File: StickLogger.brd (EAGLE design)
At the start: 61 x 61 mm, 52 parts, among them IC1 4050D, U1 ATMEGA328P-MU, U4 DS1307, X1 MICROSD, Y1 16MHZ, Y2 32.768kHz

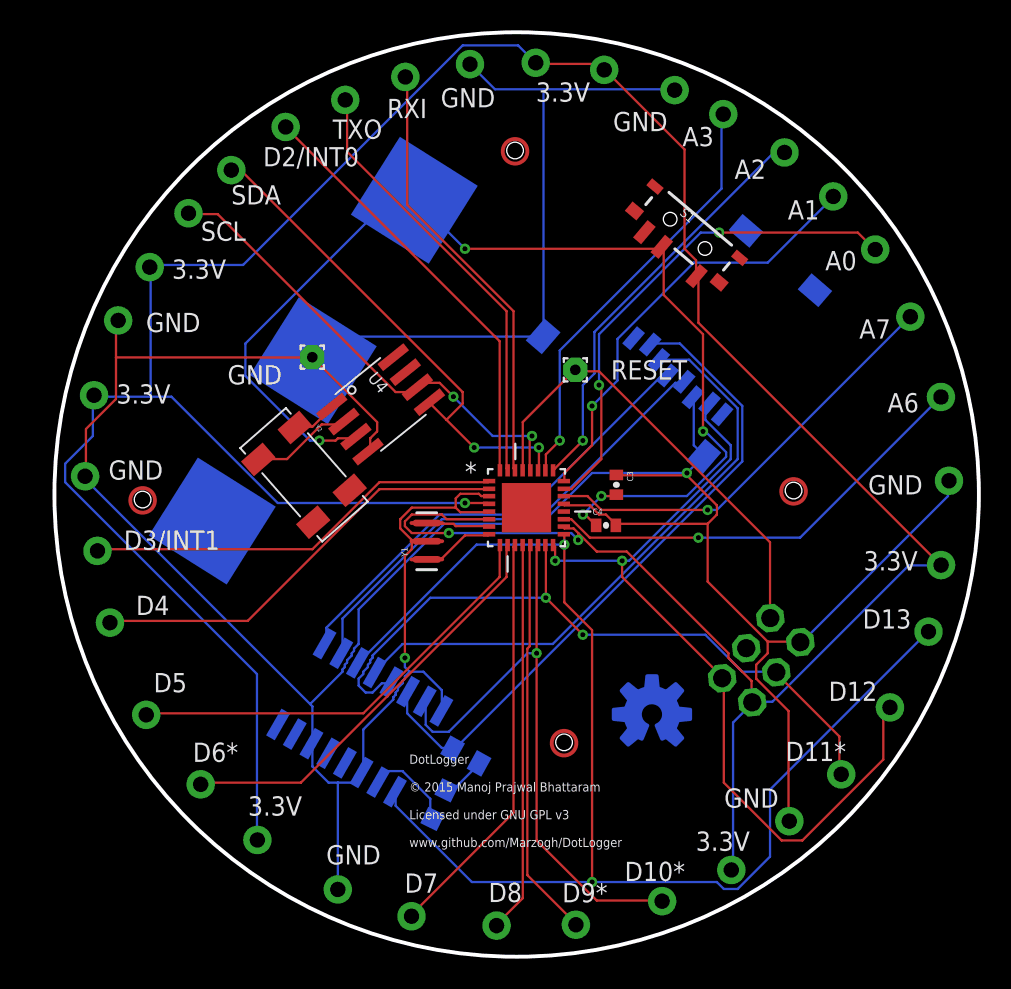
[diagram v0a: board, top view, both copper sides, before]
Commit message: Renamed project to StickLogger
New board design
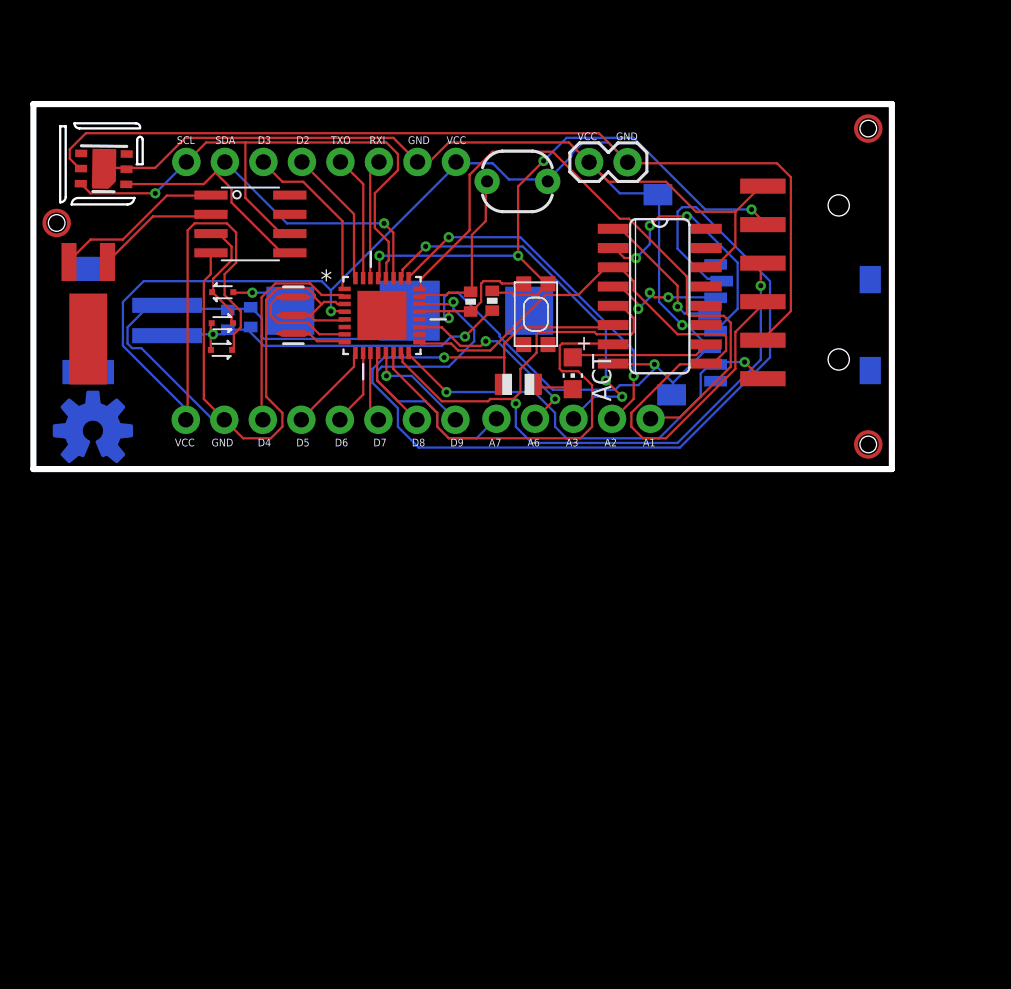
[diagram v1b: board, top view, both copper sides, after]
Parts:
- removed A0, A1, A2, A3, A6, A7, D10*, D11*, D12, D13, D2/INT0, D3/INT1, D4, D5, D6*, D7, D8, D9*, JP20, JP21, JP22, JP23, JP24, JP25, JP26, JP27, JP32, JP33, JP34, JP35, JP37, JP38, RXI, SCL, SDA, TXO: M01SMDNS, SparkFun-Connectors:1X01NS
- removed BAT1: 3.3V, SparkFun-Electromechanical:BATTCON_20MM
- removed GND: PAD-TESTPOINT, ee2parts:1,6/0,8
- removed JP6: (no value), SparkFun-Connectors:2X3_POGO
- removed S1: (no value), SparkFun-Electromechanical:SWITCH-SPST-SMD-A
- added BAT2: 3.3V, SparkFun-Electromechanical:BATTCON_12MM
- added CN1: 3.3V, adafruit:JST-PH-2-SMT-RA
- added D1, D2, D3: RB751, SparkFun-DiscreteSemi:SOD-523
- added JP1, JP2: (no value), SparkFun-Connectors:1X08_NO_SILK
- added JP3: (no value), SparkFun-Connectors:1X05_NO_SILK
- added JP4: (no value), SparkFun-Connectors:1X06-SMD
- added JP5: M02PTH, SparkFun-Connectors:1X02
- added R2: 4K7, SparkFun-Passives:0402-RES
- added R3: PHOTOCELLPTH, SparkFun-Sensors:PHOTOCELL
- added R4: 10K, SparkFun-Passives:0402-RES
- added U2: HTU21DSMD, SparkFun-Sensors:HTU21D
- RESET: value PAD-TESTPOINT -> SPST_TACT-KMR2; device ee2parts:1,6/0,8 -> adafruit:KMR2
- Y2: device microbuilder:CRYSTAL_8X3.8 -> SparkFun-FreqCtrl:CRYSTAL-32KHZ-SMD
- moved U$1 41.3 mm to (2.59, 34.9)
- moved IC1 34.1 mm to (40.0, 43.8), flipped to the top, turned to 270 degrees
- moved ACT 29.8 mm to (34.2, 38.7), flipped to the top, turned to 180 degrees
- moved C4 28.4 mm to (11.5, 42.3), flipped to the bottom, turned to 90 degrees
- moved C3 26.5 mm to (13.0, 42.4), flipped to the bottom
- moved R1 24.8 mm to (30.6, 38.0), flipped to the top, turned to 0 degrees
- moved Y2 20.0 mm to (2.29, 46.1), turned to 180 degrees
- moved Y1 17.3 mm to (15.8, 42.6)
- moved U1 15.9 mm to (21.7, 42.5)
- moved U4 14.7 mm to (13.0, 48.6), turned to 270 degrees
- moved X1 6.73 mm to (54.3, 36.9), turned to 90 degrees
- moved RESET 4.50 mm to (31.8, 42.6), turned to 90 degrees
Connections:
- removed net SCK: JP6.P$3
- new net 3V: D2.C, D3.C, U4.3
- new net AVCC: U1.18
- new net PWR: C3.2, C4.1, CN1.1, D1.A, D2.A, R2.2
- new net VCC_2: U1.6
- net A0: now also R3.1, R4.2; no longer A0.1
- net A1: now also JP3.5; no longer A1.1
- net A2: now also JP3.4; no longer A2.1
- net A3: now also JP3.3; no longer A3.1
- net A6: now also JP3.2; no longer A6.1
- net A7: now also JP3.1; no longer A7.1
- net D10*: no longer D10*.1
- net D11*: now also JP4.4; no longer D11*.1, JP6.P$4
- net D12: now also JP4.1; no longer D12.1, JP6.P$1
- net D13: now also JP4.3; no longer D13.1
- net D2/INT0: now also JP1.4; no longer D2/INT0.1
- net D3/INT1*: now also JP1.3; no longer D3/INT1.1
- net D4: now also JP2.6; no longer D4.1
- net D5*: now also JP2.5; no longer D5.1
- net D6*: now also JP2.4; no longer D6*.1
- net D7: now also JP2.3; no longer D7.1
- net D8: now also JP2.2; no longer D8.1
- net D9*: now also JP2.1; no longer D9*.1
- net DTR: now also JP4.5, R2.1, RESET.2; no longer JP6.P$5, RESET.1
- net GND: now also BAT2.GND, CN1.2, JP1.7, JP2.7, JP4.6, JP5.1, R4.1, RESET.1, U2.7, U2.GND; no longer BAT1.2, GND.1, JP22.1, JP23.1, JP26.1, JP27.1, JP33.1, JP35.1, JP38.1, JP6.P$6
- net N$6: now also Y2.X1; no longer Y2.P$1
- net N$7: now also Y2.X2; no longer Y2.P$4
- net RXI: now also JP1.6; no longer RXI.1
- net SCL: now also JP1.1, U2.SCK; no longer SCL.1
- net SDA: now also JP1.2, U2.DATA; no longer SDA.1
- net TXO: now also JP1.5; no longer TXO.1
- net VBAT: now also BAT2.PWR@1, D3.A; no longer BAT1.1, C3.2, C4.1, S1.2, U4.3
- net VCC: now also D1.C, JP1.8, JP2.8, JP4.2, JP5.2, R3.2, U2.VDD; no longer JP20.1, JP21.1, JP24.1, JP25.1, JP32.1, JP34.1, JP37.1, JP6.P$2, S1.3, U1.18, U1.6
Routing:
- net VCC: track 216.1 -> 139.0 mm, vias 3 -> 1
- net VBAT: track 73.0 -> 4.28 mm, vias 5 -> 1
- net GND: track 245.0 -> 178.3 mm, vias 2 -> 3
- net D13: track 88.5 -> 49.2 mm, vias 2 -> 0
- net N$5: track 39.7 -> 8.29 mm, vias 0 -> 3
- net N$3: track 43.9 -> 71.1 mm, vias 0 -> 1
- net D12: track 55.4 -> 29.7 mm
- net PWR: track 0.00 -> 25.5 mm, vias 0 -> 2
- net D5*: track 29.2 -> 5.87 mm
- net D6*: track 28.0 -> 5.04 mm
- net D7: track 27.3 -> 4.62 mm
- net A0: track 33.0 -> 11.3 mm, vias 2 -> 0
- net RXI: track 29.0 -> 7.92 mm
- net +3V3: track 30.5 -> 9.48 mm, vias 0 -> 1
- net TXO: track 28.9 -> 8.30 mm
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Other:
- board size 61 x 61 mm -> 56.6 x 24.1 mm
- board text added: "A1"
- board text added: "A2"
- board text added: "A3"
- board text added: "A6"
- board text added: "A7"
- board text added: "D2"
- board text added: "D3"
- board text added: "D4"
- board text added: "D5"
- board text added: "D6"
- board text added: "D7"
- board text added: "D8"
- board text added: "D9"
- board text added: "RXI"
- board text added: "SCL"
- board text added: "SDA"
- board text added: "StickLogger"
- board text added: "StickLogger (GNU GPL v3) © 2015 Manoj Prajwal Bhattaram www.github.com/Marzogh/StickLogger"
- board text added: "TXO"
- board text added: "VCC"
- board text removed: "3.3V"
- board text removed: "DotLogger"
- board text removed: "DotLogger © 2015 Manoj Prajwal Bhattaram Licensed under GNU GPL v3 www.github.com/Marzogh/DotLogger"
